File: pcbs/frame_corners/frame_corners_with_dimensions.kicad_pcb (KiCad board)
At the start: 2 copper layers, 53.6 x 40 mm, 8 parts

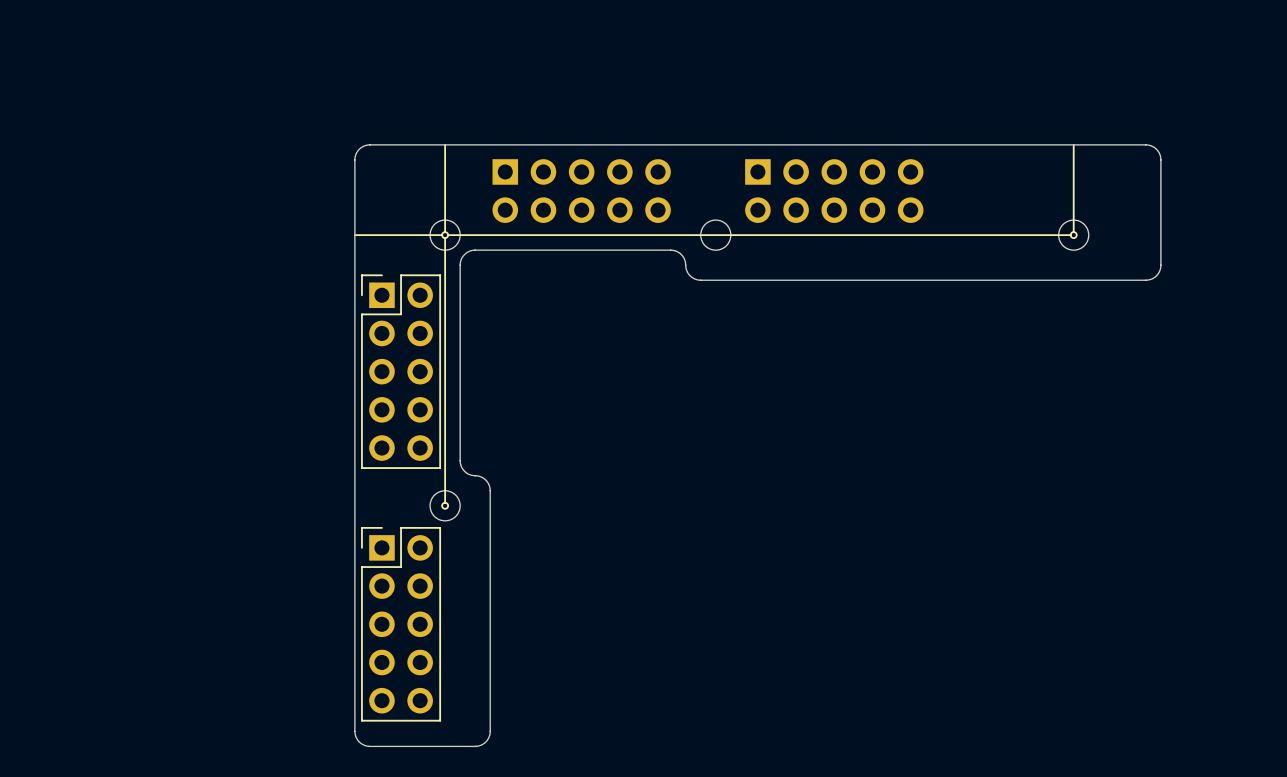
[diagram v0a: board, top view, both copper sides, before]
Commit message: Panelization with https://gitlab.com/dren.dk/kicad-util
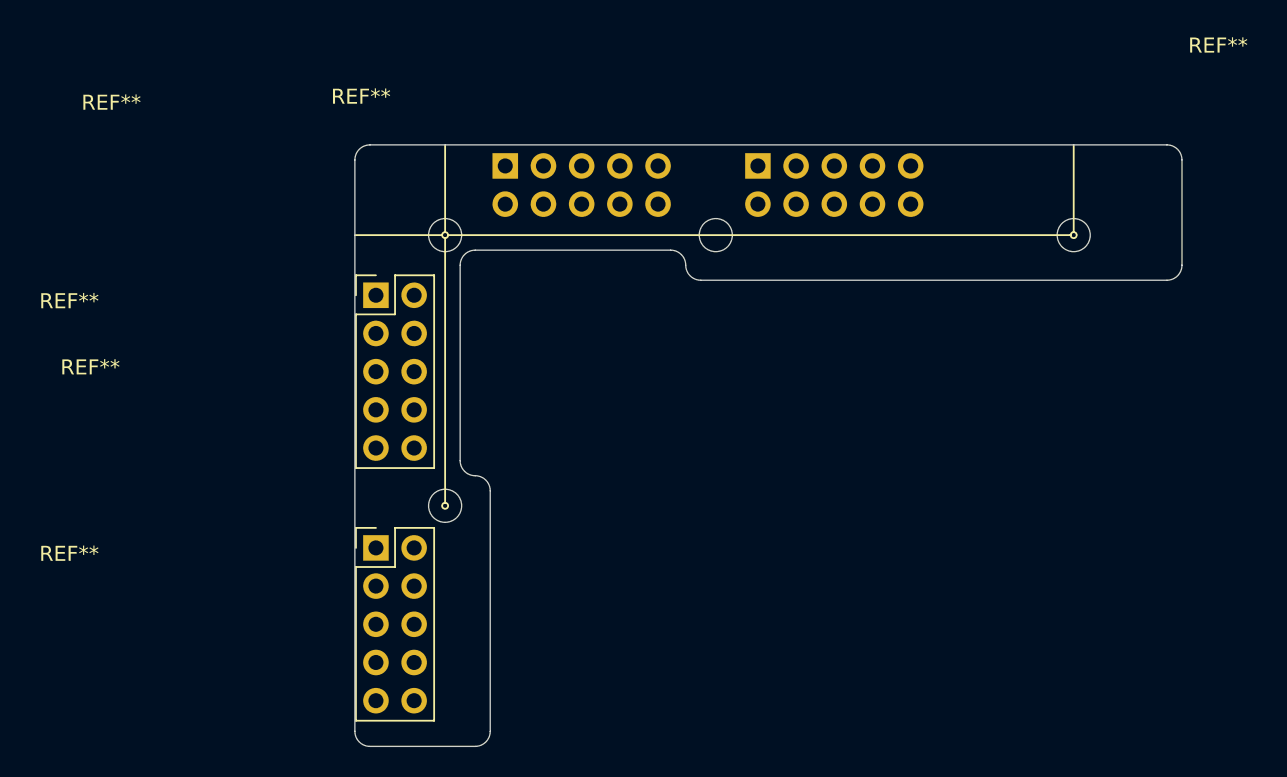
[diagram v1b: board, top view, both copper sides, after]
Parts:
- removed the REF** at (145.3, 99.0)
- removed the REF** at (153.5, 90.8)
- added REF**: PinHeader_2x05_P2.54mm_Vertical, Connector_PinHeader_2.54mm:PinHeader_2x05_P2.54mm_Vertical, F.Cu at (144.9, 99.0)
- added REF**: PinHeader_2x05_P2.54mm_Vertical, Connector_PinHeader_2.54mm:PinHeader_2x05_P2.54mm_Vertical, B.Cu at (153.5, 90.4)
- moved REF** 0.40 mm to (170.3, 90.4)
- moved REF** 0.40 mm to (144.9, 115.8)
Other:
- board size 53.6 x 40 mm -> 55 x 40 mm
